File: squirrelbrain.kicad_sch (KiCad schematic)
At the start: 20 parts, among them J1 Conn_01x01, J2 Conn_01x01, J3 Conn_01x03, J4 Conn_01x02, J5 Conn_01x02, Q1 SISS80DN-T1-GE3, U1 SEEEDUINO-XIAO-ESP32S3, U2 THVD1420DRLR, U3 THVD1420DRLR, U5 RPM5.0-6.0, U6 SN74LVC2G125DCUR

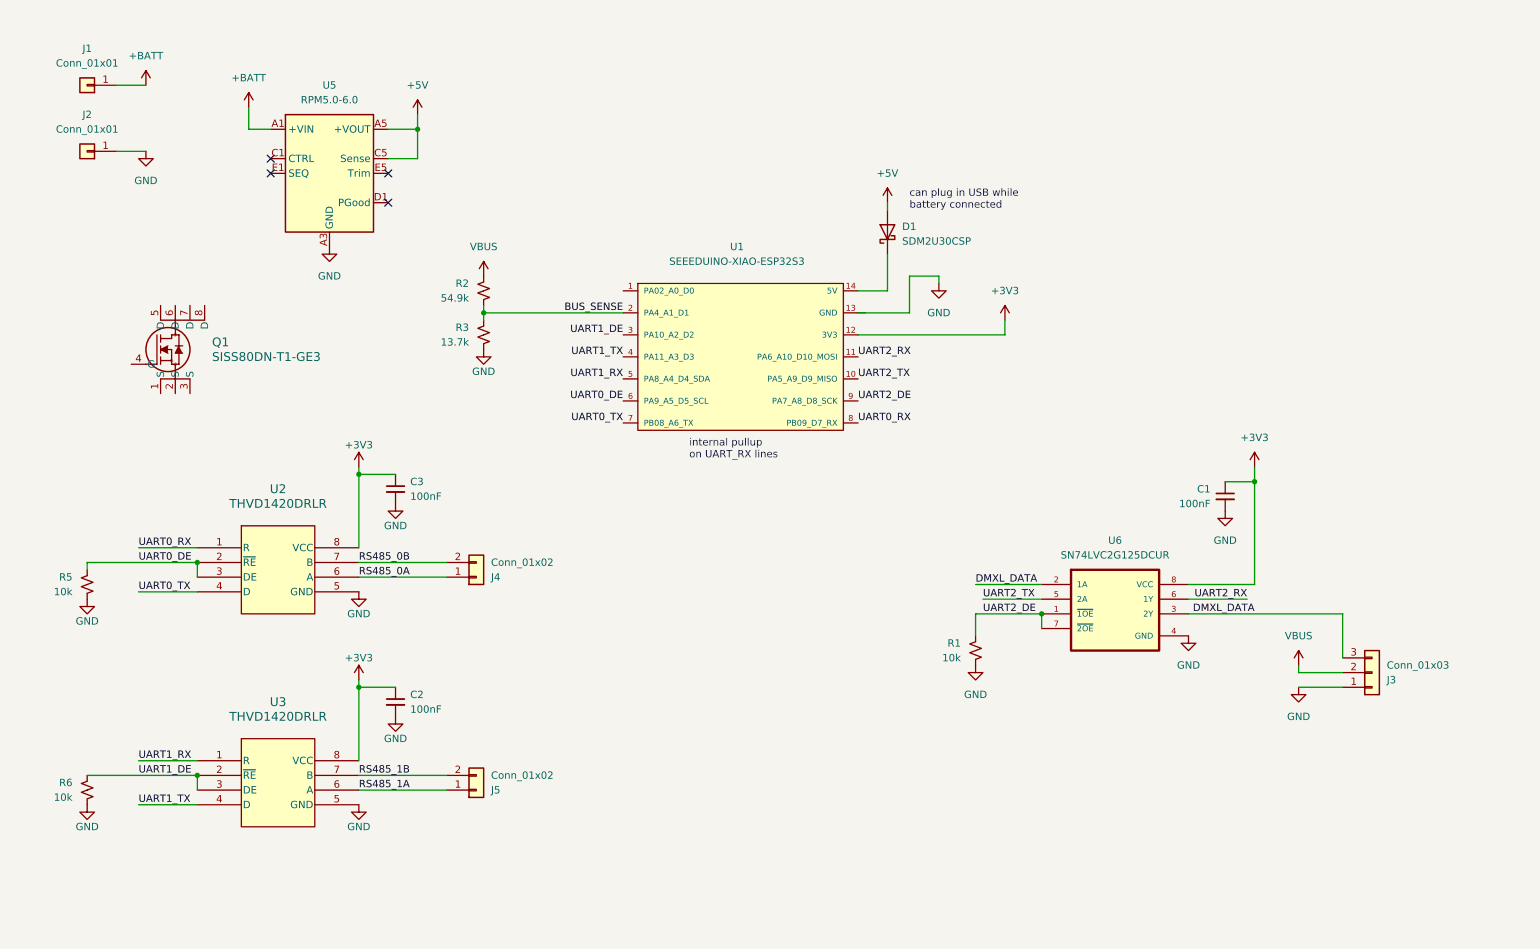
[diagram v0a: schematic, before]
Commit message: chose high side load switches
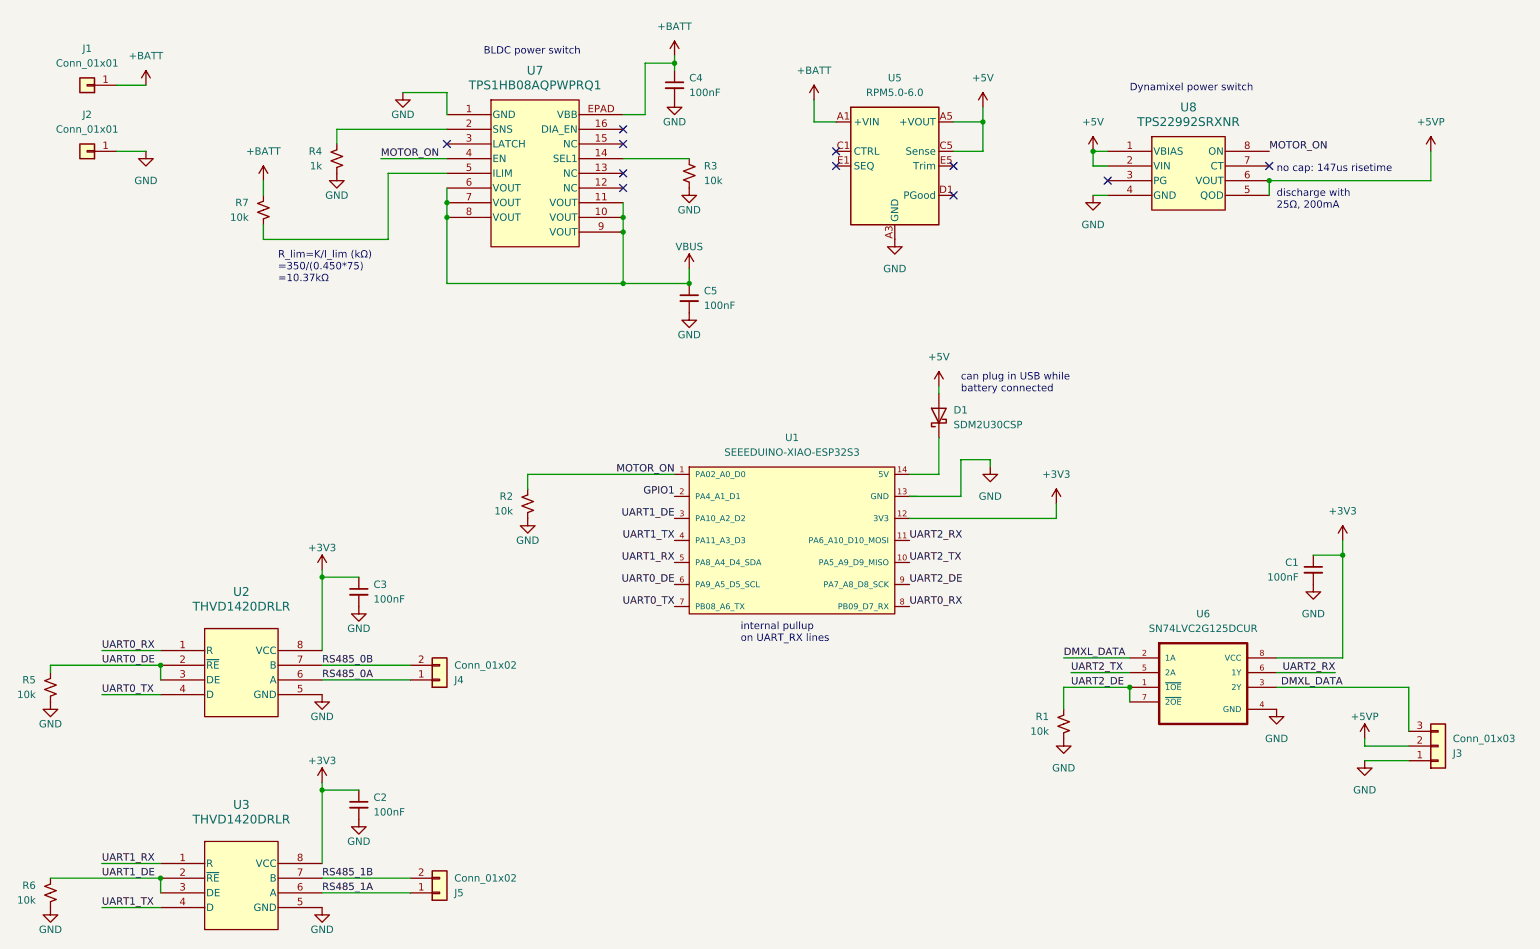
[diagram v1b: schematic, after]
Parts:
- removed Q1: SISS80DN-T1-GE3, squirrelbrain:SISS80DN, symbol squirrelbrain:SISS80DN-T1-GE3
- added C4, C5: 100nF, Capacitor_SMD:C_0402_1005Metric, symbol Device:C_Small
- added R4: 1k, Resistor_SMD:R_0402_1005Metric, symbol Device:R_Small_US
- added R7: 10k, Resistor_SMD:R_0402_1005Metric, symbol Device:R_Small_US
- added U7: TPS1HB08AQPWPRQ1, squirrelbrain:TPS1HB08, symbol squirrelbrain:TPS1HB08AQPWPRQ1
- added U8: TPS22992SRXNR, squirrelbrain:TPS22992S, symbol squirrelbrain:TPS22992SRXNR
- R2: value 54.9k -> 10k
- R3: value 13.7k -> 10k
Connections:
- net +5V: now also U8.1 (VBIAS), U8.2 (VIN)
- net +BATT: now also C4.1, R7.2, U7.EPAD (VBB)
- net GND: now also R2.1, C4.2, C5.2, R4.1, U7.1 (GND), U8.4 (GND)
- net VBUS: now also C5.1, U7.10 (VOUT), U7.11 (VOUT), U7.6 (VOUT), U7.7 (VOUT), U7.8 (VOUT), U7.9 (VOUT); no longer J3.2 (Pin_2), R2.2
- net MOTOR_ON: now reaches U1.1 (PA02_A0_D0)
- net MOTOR_ON: now also R2.2, U7.4 (EN), U8.8 (ON)
- removed net BUS_SENSE: R2.1, R3.2, U1.2 (PA4_A1_D1)
- new net: R4.2, U7.2 (SNS)
- new net: R3.2, U7.14 (SEL1)
- new net: R7.1, U7.5 (ILIM)
- new net +5VP: J3.2 (Pin_2), U8.5 (QOD), U8.6 (VOUT)
- new net GPIO1: U1.2 (PA4_A1_D1)
- no-connect marks 4 -> 11
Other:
- note added: "BLDC power switch"
- note added: "Dynamixel power switch"
- note added: "R_lim=K/I_lim (kΩ) =350/(0.450*75) =10.37kΩ"
- note added: "discharge with 25Ω, 200mA"
- note added: "no cap: 147us risetime"
- moved on the sheet: C1, C2, C3, D1, J3, J4, J5, R1, R5, R6, U1, U2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

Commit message: add xt30, start routing
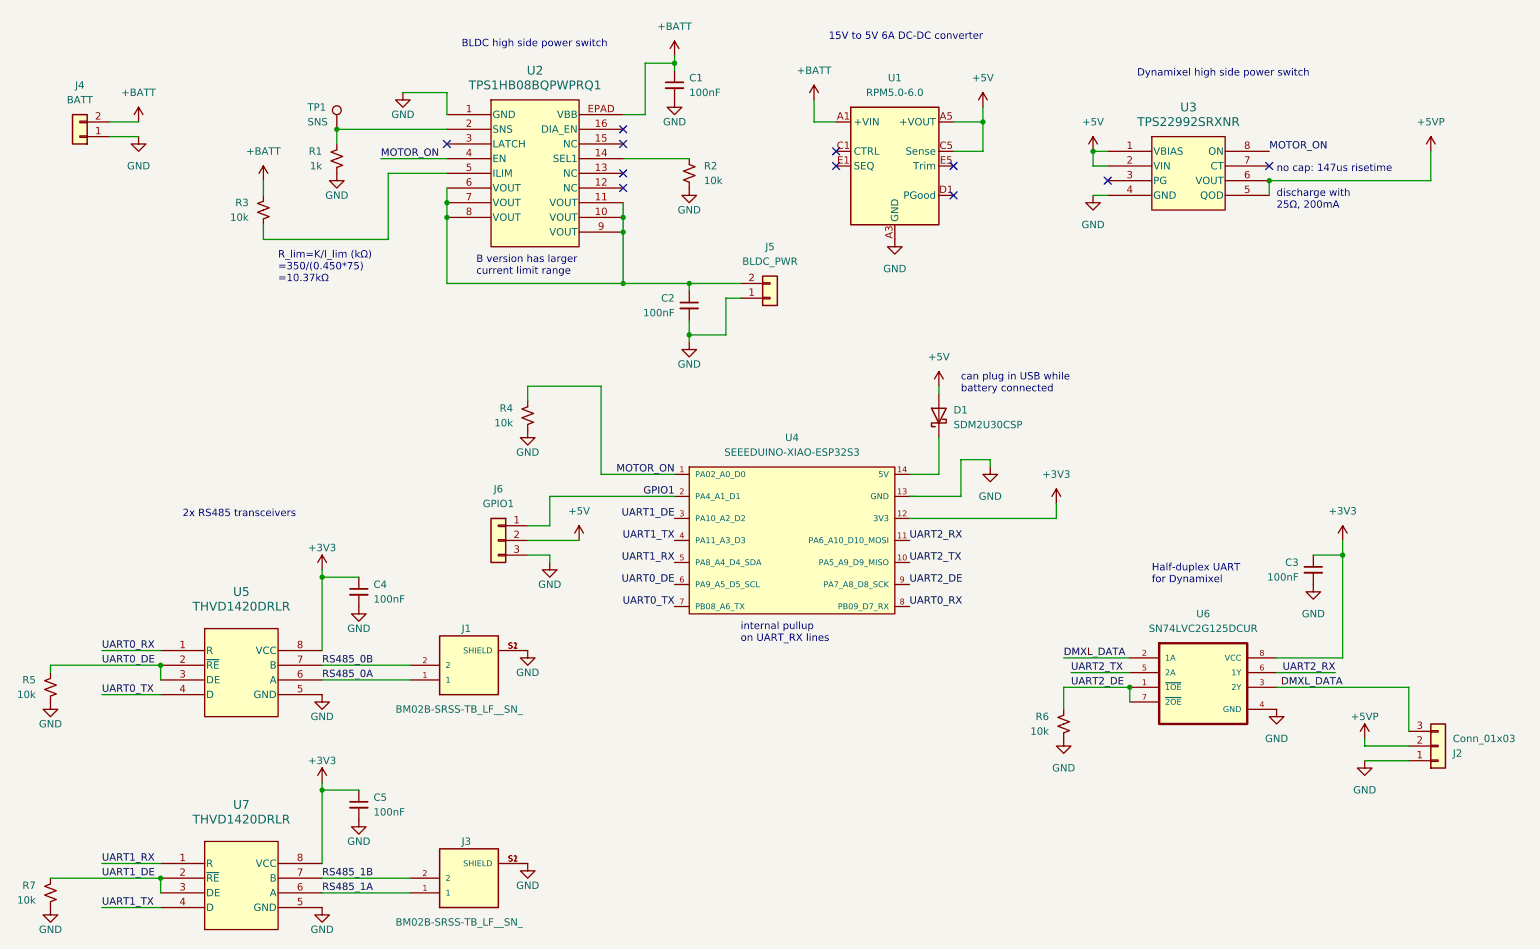
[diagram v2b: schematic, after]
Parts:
- removed J1, J2: Conn_01x01, Connector_Wire:SolderWire-0.1sqmm_1x01_D0.4mm_OD1mm, symbol Connector_Generic:Conn_01x01
- added J1, J3: BM02B-SRSS-TB_LF__SN_, squirrelbrain:JST_BM02B-SRSS-TB_LF__SN_, symbol squirrelbrain:BM02B-SRSS-TB_LF__SN_
- added J6: GPIO1, Connector_PinSocket_2.54mm:PinSocket_1x03_P2.54mm_Vertical, symbol Connector_Generic:Conn_01x03
- added TP1: SNS, TestPoint:TestPoint_Pad_1.0x1.0mm, symbol Connector:TestPoint
- J4: value Conn_01x02 -> BATT; footprint squirrelbrain:JST_SM02B-SRSS-TB(LF)(SN) -> squirrelbrain:AMASS_XT30U-M_1x02_P5.0mm_Vertical
- J5: value Conn_01x02 -> BLDC_PWR; footprint squirrelbrain:JST_SM02B-SRSS-TB(LF)(SN) -> squirrelbrain:AMASS_XT30U-F_1x02_P5.0mm_Vertical
- U2: renamed from U7; value TPS1HB08AQPWPRQ1 -> TPS1HB08BQPWPRQ1
- renumbered C4 to C1, C5 to C2, C1 to C3, C3 to C4, C2 to C5, J3 to J2, R4 to R1, R3 to R2, R7 to R3, R2 to R4, R1 to R6, R6 to R7, U5 to U1, U8 to U3, U1 to U4, U2 to U5, U3 to U7
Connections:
- net +5V: now also J6.2 (Pin_2)
- net +BATT: now also J4.2 (Pin_2)
- net GND: now also J4.1 (Pin_1), J5.1 (Pin_1), J1.S1 (SHIELD), J1.S2 (SHIELD), J3.S1 (SHIELD), J3.S2 (SHIELD), J6.3 (Pin_3)
- net GPIO1: now also J6.1 (Pin_1)
- net RS485_0A: now also J1.1; no longer J4.1 (Pin_1)
- net RS485_0B: now also J1.2; no longer J4.2 (Pin_2)
- net RS485_1A: now also J3.1; no longer J5.1 (Pin_1)
- net RS485_1B: now also J3.2; no longer J5.2 (Pin_2)
- net at R1.2, U2.2 (SNS): now also TP1.1
- net VBUS: no longer names the net of C2.1, U2.10 (VOUT), U2.11 (VOUT), U2.6 (VOUT), U2.7 (VOUT), U2.8 (VOUT), U2.9 (VOUT)
- net VBUS: now also J5.2 (Pin_2)
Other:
- note added: "15V to 5V 6A DC-DC converter"
- note added: "2x RS485 transceivers"
- note added: "B version has larger current limit range"
- note added: "BLDC high side power switch"
- note added: "Dynamixel high side power switch"
- note added: "Half-duplex UART for Dynamixel"
- note removed: "BLDC power switch"
- note removed: "Dynamixel power switch"
- moved on the sheet: C2, R4

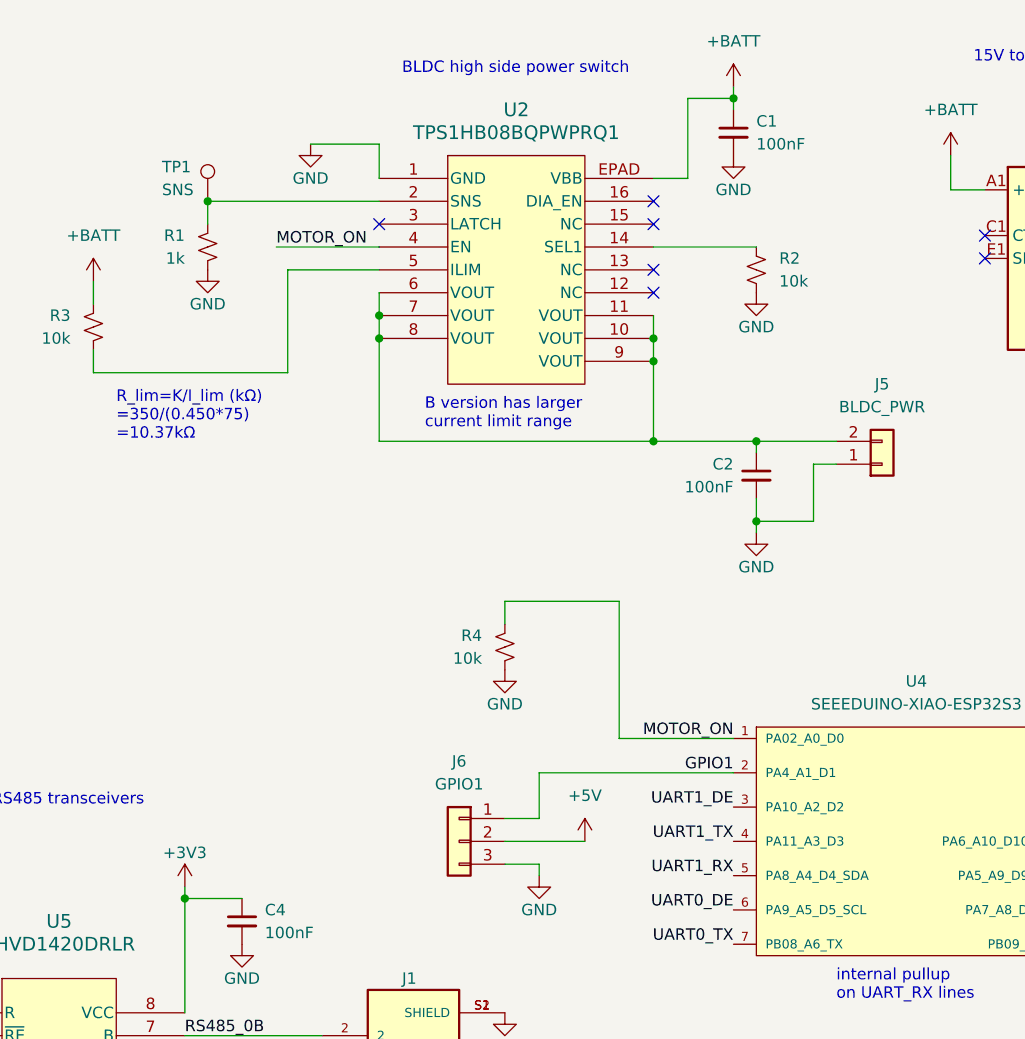
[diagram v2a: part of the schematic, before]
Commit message: finished routing? need to add 3v3 breakout
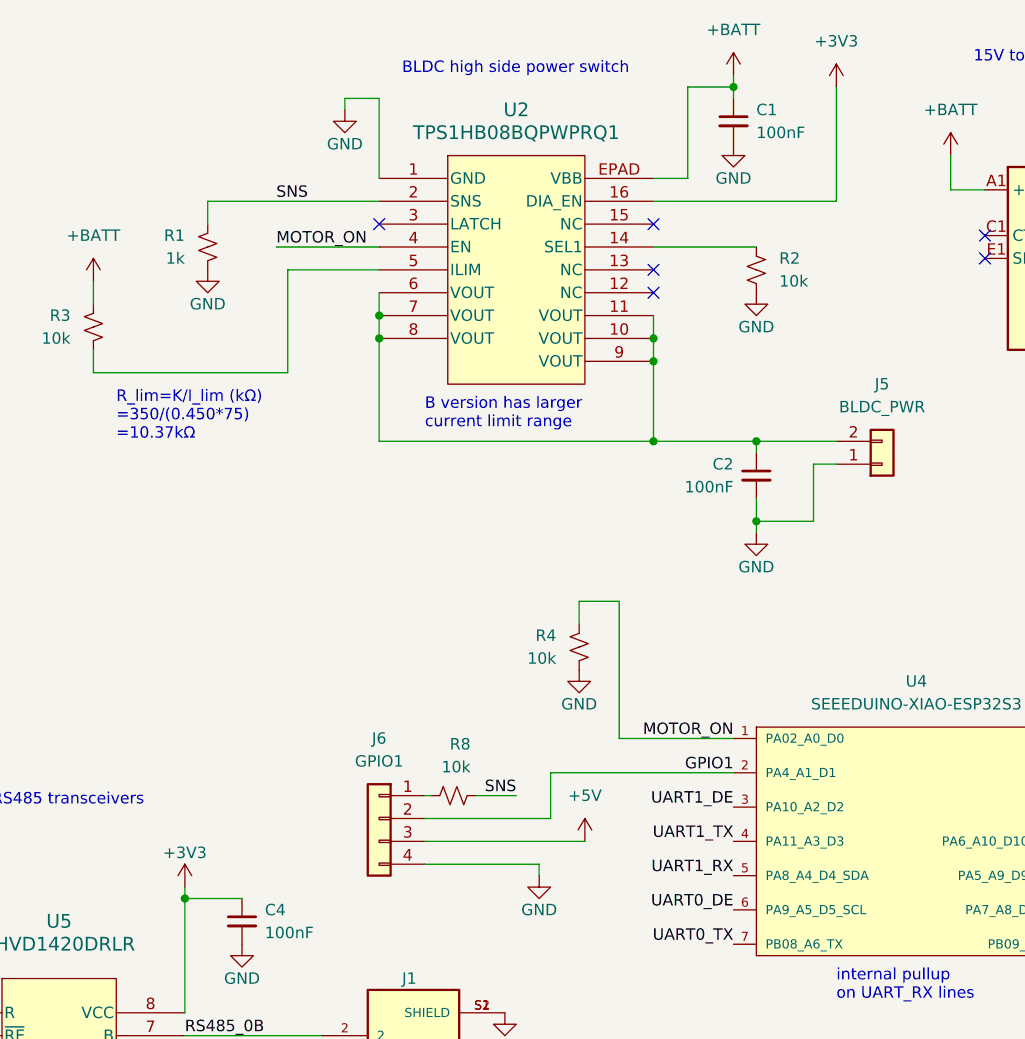
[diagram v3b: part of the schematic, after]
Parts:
- removed TP1: SNS, TestPoint:TestPoint_Pad_1.0x1.0mm, symbol Connector:TestPoint
- added R8: 10k, Resistor_SMD:R_0402_1005Metric, symbol Device:R_Small_US
- C1, C2, C3, C4, C5: MP (none) -> CL05A104KA5NNNC; Vendor (none) -> Digikey
- D1: MP (none) -> SDM2U30CSP-7
- J2: MP (none) -> B3B-EH-A; Vendor (none) -> Digikey; Vendor # (none) -> 455-B3B-EH-A-ND
- J4: MP (none) -> XT30U-M
- J5: MP (none) -> XT30U-F
- J6: footprint Connector_PinSocket_2.54mm:PinSocket_1x03_P2.54mm_Vertical -> Connector_PinSocket_2.54mm:PinSocket_1x04_P2.54mm_Vertical; symbol Connector_Generic:Conn_01x03 -> Connector_Generic:Conn_01x04
- R1: MP (none) -> RC0402FR-071KL; Vendor (none) -> Digikey; Vendor # (none) -> 311-1.00KLRCT-ND
- R2, R3, R4, R5, R6, R7: MP (none) -> RC0402FR-0710KL; Vendor (none) -> Digikey; Vendor # (none) -> 311-10.0KLRCT-ND
- U1: MP (none) -> RPM5.0-6.0; Vendor (none) -> Digikey; Vendor # (none) -> 945-RPM5.0-6.0CT-ND
- U2: MP (none) -> TPS1HB08BQPWPRQ1; Vendor (none) -> Digikey; Vendor # (none) -> 296-TPS1HB08BQPWPRQ1CT-ND
- U3: MP (none) -> TPS22992SRXNR; Vendor (none) -> Digikey; Vendor # (none) -> 296-TPS22992SRXNRCT-ND
- U5, U7: MP (none) -> THVD1420DRLR; Vendor (none) -> Digikey; Vendor # (none) -> 296-THVD1420DRLRCT-ND
- U6: MP (none) -> SN74LVC2G125DCUR; Vendor (none) -> Digikey; Vendor # (none) -> 296-13265-1-ND
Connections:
- net +3V3: now also U2.16 (DIA_EN)
- net +5V: now also J6.3 (Pin_3); no longer J6.2 (Pin_2)
- net GND: now also J6.4 (Pin_4); no longer J6.3 (Pin_3)
- net GPIO1: now also J6.2 (Pin_2); no longer J6.1 (Pin_1)
- net SNS: now reaches R1.2, U2.2 (SNS)
- net SNS: now also R8.1
- new net: J6.1 (Pin_1), R8.2
- no-connect marks 11 -> 10
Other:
- moved on the sheet: C1, R4
